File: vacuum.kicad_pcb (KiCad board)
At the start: 2 copper layers, 28 parts, among them J1 нагрузка, J2 нагрузка, J3 нагрузка, J4 геркон клапана 0, J5 геркон клапана 1, J6 геркон шибера 0, J7 геркон шибера 1, Q1 IRF740, Q2 IRF740, Q3 IRF740, SW1 Кнопка, SW2 Кнопка, SW3 Кнопка, SW4 Выключить автоматику

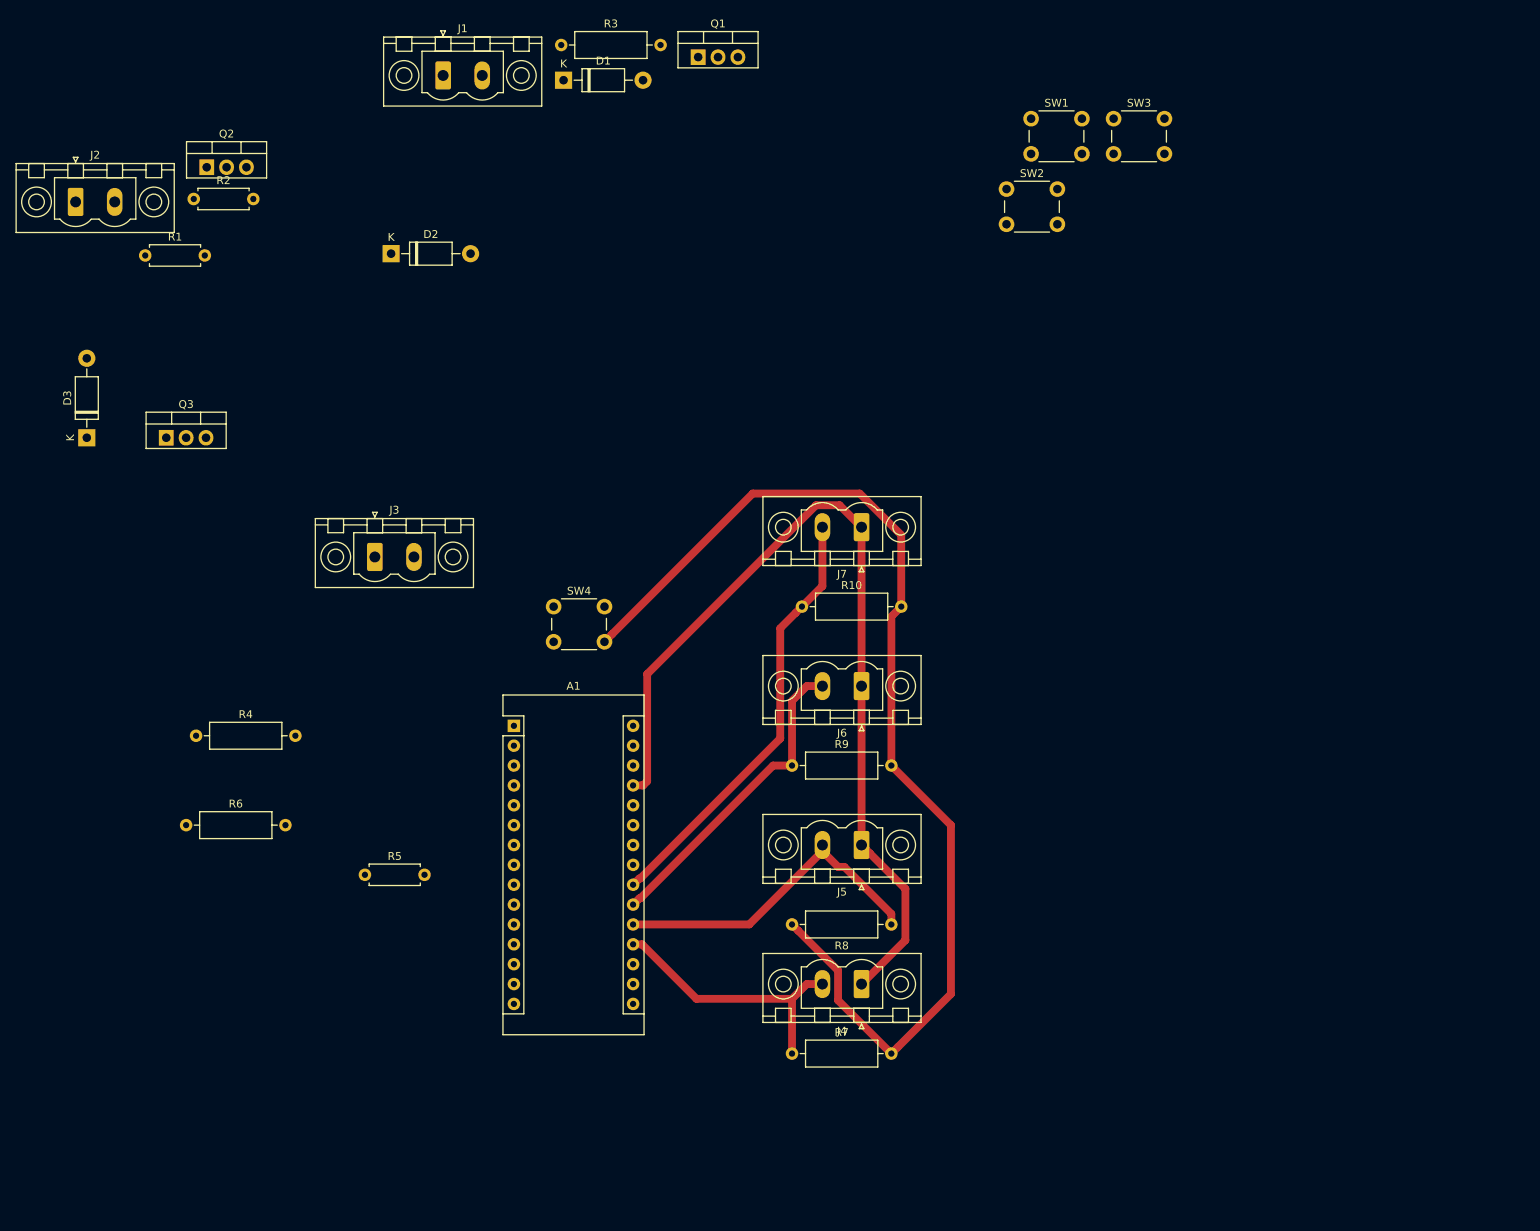
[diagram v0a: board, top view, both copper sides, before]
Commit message: common - for power supply added, terminals to power supply added
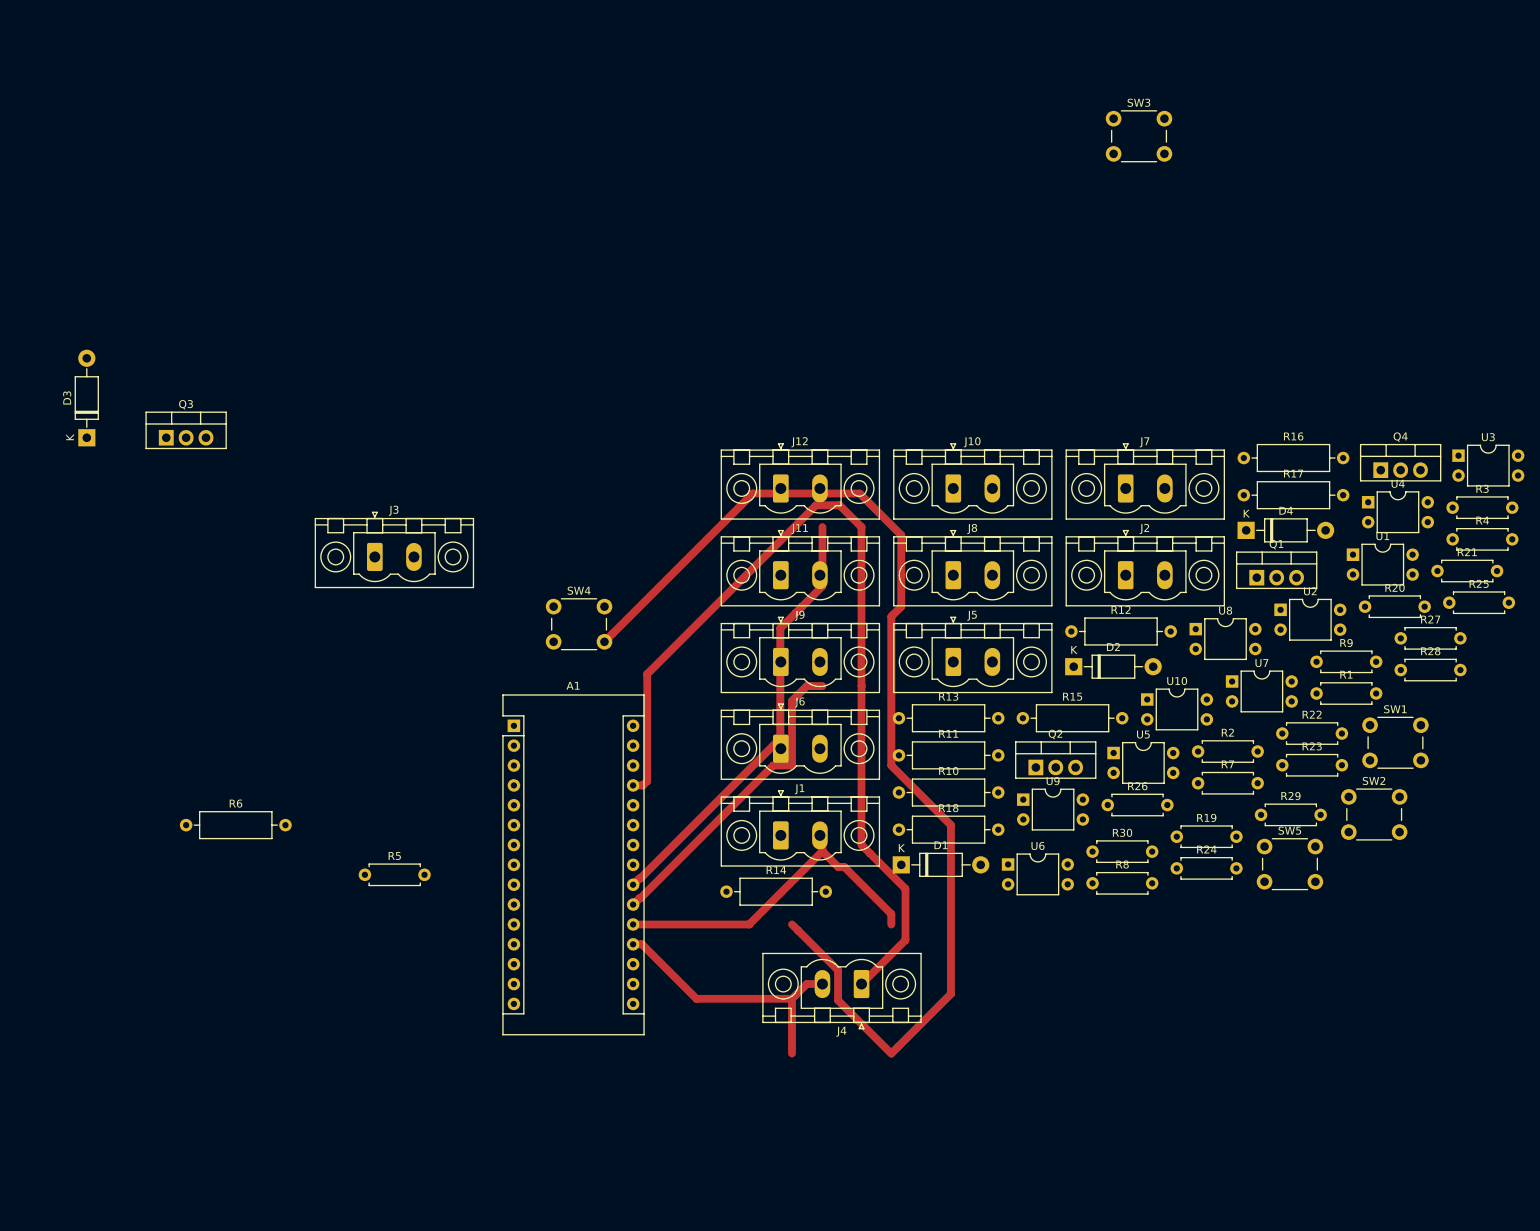
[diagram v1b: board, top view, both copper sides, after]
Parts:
- added D4: 1N4001, Diode_THT:D_DO-41_SOD81_P10.16mm_Horizontal, F.Cu at (206.7, 79.2)
- added J10: геркон шибера 1, Connector_Phoenix_MSTB:PhoenixContact_MSTBV_2,5_2-GF_1x02_P5.00mm_Vertical_ThreadedFlange, F.Cu at (169.2, 73.8)
- added J11: запасной, Connector_Phoenix_MSTB:PhoenixContact_MSTBV_2,5_2-GF_1x02_P5.00mm_Vertical_ThreadedFlange, F.Cu at (147.2, 84.9)
- added J12: запасной, Connector_Phoenix_MSTB:PhoenixContact_MSTBV_2,5_2-GF_1x02_P5.00mm_Vertical_ThreadedFlange, F.Cu at (147.2, 73.8)
- added J8: геркон клапана 1, Connector_Phoenix_MSTB:PhoenixContact_MSTBV_2,5_2-GF_1x02_P5.00mm_Vertical_ThreadedFlange, F.Cu at (169.2, 84.9)
- added J9: геркон шибера 0, Connector_Phoenix_MSTB:PhoenixContact_MSTBV_2,5_2-GF_1x02_P5.00mm_Vertical_ThreadedFlange, F.Cu at (147.2, 96.0)
- added Q4: IRF740, Package_TO_SOT_THT:TO-220-3_Vertical, F.Cu at (223.9, 71.5)
- added R11: 10k, Resistor_THT:R_Axial_DIN0309_L9.0mm_D3.2mm_P12.70mm_Horizontal, F.Cu at (162.3, 107.9)
- added R12: 10k, Resistor_THT:R_Axial_DIN0309_L9.0mm_D3.2mm_P12.70mm_Horizontal, F.Cu at (184.3, 92.1)
- added R13: 10k, Resistor_THT:R_Axial_DIN0309_L9.0mm_D3.2mm_P12.70mm_Horizontal, F.Cu at (162.3, 103.2)
- added R14: 10k, Resistor_THT:R_Axial_DIN0309_L9.0mm_D3.2mm_P12.70mm_Horizontal, F.Cu at (140.2, 125.3)
- added R15: 10k, Resistor_THT:R_Axial_DIN0309_L9.0mm_D3.2mm_P12.70mm_Horizontal, F.Cu at (178.1, 103.2)
- added R16: 10k, Resistor_THT:R_Axial_DIN0309_L9.0mm_D3.2mm_P12.70mm_Horizontal, F.Cu at (206.4, 69.9)
- added R17: 10k, Resistor_THT:R_Axial_DIN0309_L9.0mm_D3.2mm_P12.70mm_Horizontal, F.Cu at (206.4, 74.7)
- added R18: 10k, Resistor_THT:R_Axial_DIN0309_L9.0mm_D3.2mm_P12.70mm_Horizontal, F.Cu at (162.3, 117.4)
- added R19: 470, Resistor_THT:R_Axial_DIN0207_L6.3mm_D2.5mm_P7.62mm_Horizontal, F.Cu at (197.8, 118.3)
- added R20: 470, Resistor_THT:R_Axial_DIN0207_L6.3mm_D2.5mm_P7.62mm_Horizontal, F.Cu at (221.9, 88.9)
- added R21: 470, Resistor_THT:R_Axial_DIN0207_L6.3mm_D2.5mm_P7.62mm_Horizontal, F.Cu at (231.1, 84.3)
- added R22: 470, Resistor_THT:R_Axial_DIN0207_L6.3mm_D2.5mm_P7.62mm_Horizontal, F.Cu at (211.3, 105.1)
- added R23: 470, Resistor_THT:R_Axial_DIN0207_L6.3mm_D2.5mm_P7.62mm_Horizontal, F.Cu at (211.3, 109.2)
- added R24: 470, Resistor_THT:R_Axial_DIN0207_L6.3mm_D2.5mm_P7.62mm_Horizontal, F.Cu at (197.8, 122.4)
- added R25: 470, Resistor_THT:R_Axial_DIN0207_L6.3mm_D2.5mm_P7.62mm_Horizontal, F.Cu at (232.6, 88.4)
- added R26: 470, Resistor_THT:R_Axial_DIN0207_L6.3mm_D2.5mm_P7.62mm_Horizontal, F.Cu at (189.0, 114.3)
- added R27: 470, Resistor_THT:R_Axial_DIN0207_L6.3mm_D2.5mm_P7.62mm_Horizontal, F.Cu at (226.4, 93.0)
- added R28: 470, Resistor_THT:R_Axial_DIN0207_L6.3mm_D2.5mm_P7.62mm_Horizontal, F.Cu at (226.4, 97.0)
- added R29: 470, Resistor_THT:R_Axial_DIN0207_L6.3mm_D2.5mm_P7.62mm_Horizontal, F.Cu at (208.6, 115.5)
- added R30: 470, Resistor_THT:R_Axial_DIN0207_L6.3mm_D2.5mm_P7.62mm_Horizontal, F.Cu at (187.0, 120.2)
- added SW5: Кнопка, Button_Switch_THT:SW_PUSH_6mm_H5mm, F.Cu at (209.0, 119.6)
- added U1: PC817, Package_DIP:DIP-4_W7.62mm, F.Cu at (220.3, 82.3)
- added U10: PC817, Package_DIP:DIP-4_W7.62mm, F.Cu at (194.0, 100.8)
- added U2: PC817, Package_DIP:DIP-4_W7.62mm, F.Cu at (211.1, 89.3)
- added U3: PC817, Package_DIP:DIP-4_W7.62mm, F.Cu at (233.8, 69.6)
- added U4: PC817, Package_DIP:DIP-4_W7.62mm, F.Cu at (222.3, 75.6)
- added U5: PC817, Package_DIP:DIP-4_W7.62mm, F.Cu at (189.7, 107.6)
- added U6: PC817, Package_DIP:DIP-4_W7.62mm, F.Cu at (176.2, 121.9)
- added U7: PC817, Package_DIP:DIP-4_W7.62mm, F.Cu at (204.9, 98.5)
- added U8: PC817, Package_DIP:DIP-4_W7.62mm, F.Cu at (200.2, 91.8)
- added U9: PC817, Package_DIP:DIP-4_W7.62mm, F.Cu at (178.2, 113.6)
- J1: value нагрузка -> к БП
- J5: value геркон клапана 1 -> нагрузка
- J6: value геркон шибера 0 -> нагрузка
- J7: value геркон шибера 1 -> к БП
- R1, R2, R5: value 100 -> 470
- R3, R4, R7, R8, R9: value 10k -> 470; footprint Resistor_THT:R_Axial_DIN0309_L9.0mm_D3.2mm_P12.70mm_Horizontal -> Resistor_THT:R_Axial_DIN0207_L6.3mm_D2.5mm_P7.62mm_Horizontal
- moved R4 162.6 mm to (233.1, 80.3)
- moved R1 159.9 mm to (215.7, 100.0)
- moved R2 146.6 mm to (200.5, 107.4)
- moved J2 142.5 mm to (191.3, 84.9)
- moved Q2 130.9 mm to (179.8, 109.5)
- moved R3 128.4 mm to (233.1, 76.2)
- moved D1 109.2 mm to (162.6, 121.9)
- moved J1 106.3 mm to (147.2, 118.2)
- moved D2 102.0 mm to (184.6, 96.6)
- moved Q1 97.6 mm to (208.0, 85.2)
- moved SW2 89.2 mm to (219.8, 113.2)
- moved SW1 88.8 mm to (222.5, 104.1)
- moved R9 68.4 mm to (215.7, 96.0)
- moved R7 62.4 mm to (200.5, 111.5)
- moved J7 34.1 mm to (191.3, 73.8), turned to 0 degrees
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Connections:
- A1 pad 19: Net-(A1-Pad19) -> (no net)
- A1 pad 23: (no net) -> Net-(A1-Pad23)
- A1 pad 24: (no net) -> Net-(A1-Pad24)
- A1 pad 25: (no net) -> Net-(A1-Pad25)
- A1 pad 4: Earth -> Net-(A1-Pad4)
- A1 pad 6: (no net) -> Net-(A1-Pad6)
- D2 pad 1: Net-(D2-Pad1) -> Net-(D1-Pad1)
- D3 pad 2: Net-(D2-Pad1) -> Net-(D3-Pad2)
- J1 pad 1: +24V -> Earth
- J1 pad 2: Net-(D1-Pad2) -> +24V
- J2 pad 2: Net-(D2-Pad2) -> Net-(D1-Pad2)
- J3 pad 2: Net-(D2-Pad1) -> Net-(D3-Pad2)
- J4 pad 1: +5V -> Net-(J4-Pad1)
- J4 pad 2: Net-(A1-Pad19) -> Earth
- J5 pad 1: +5V -> +24V
- J5 pad 2: Net-(A1-Pad20) -> Net-(D2-Pad2)
- J6 pad 1: +5V -> +24V
- J6 pad 2: Net-(A1-Pad21) -> Net-(D4-Pad2)
- J7 pad 1: +5V -> Earth
- J7 pad 2: Net-(A1-Pad22) -> +5V
- Q2 pad 3: Net-(D2-Pad1) -> Net-(D1-Pad1)
- Q3 pad 2: Net-(D2-Pad1) -> Net-(D3-Pad2)
- R1 pad 2: Net-(A1-Pad9) -> +5V
- R10 pad 1: Net-(A1-Pad22) -> Net-(A1-Pad6)
- R10 pad 2: Earth -> Net-(A1-Pad4)
- R2 pad 2: Net-(A1-Pad11) -> +5V
- R3 pad 1: Net-(A1-Pad9) -> Net-(Q4-Pad1)
- R3 pad 2: Net-(D1-Pad1) -> +5V
- R4 pad 1: Net-(A1-Pad11) -> Net-(R4-Pad1)
- R4 pad 2: Net-(D2-Pad1) -> Net-(A1-Pad6)
- R5 pad 2: Net-(A1-Pad13) -> +5V
- R6 pad 2: Net-(D1-Pad1) -> Net-(A1-Pad4)
- R7 pad 1: Net-(A1-Pad19) -> Net-(R7-Pad1)
- R7 pad 2: Earth -> Net-(A1-Pad9)
- R8 pad 1: Net-(A1-Pad20) -> Net-(R8-Pad1)
- R8 pad 2: Earth -> Net-(A1-Pad11)
- R9 pad 1: Net-(A1-Pad21) -> Net-(R9-Pad1)
- R9 pad 2: Earth -> Net-(A1-Pad13)
- SW2 pad 1: Net-(D2-Pad1) -> Earth
- SW3 pad 2: Net-(D2-Pad1) -> Net-(D3-Pad2)

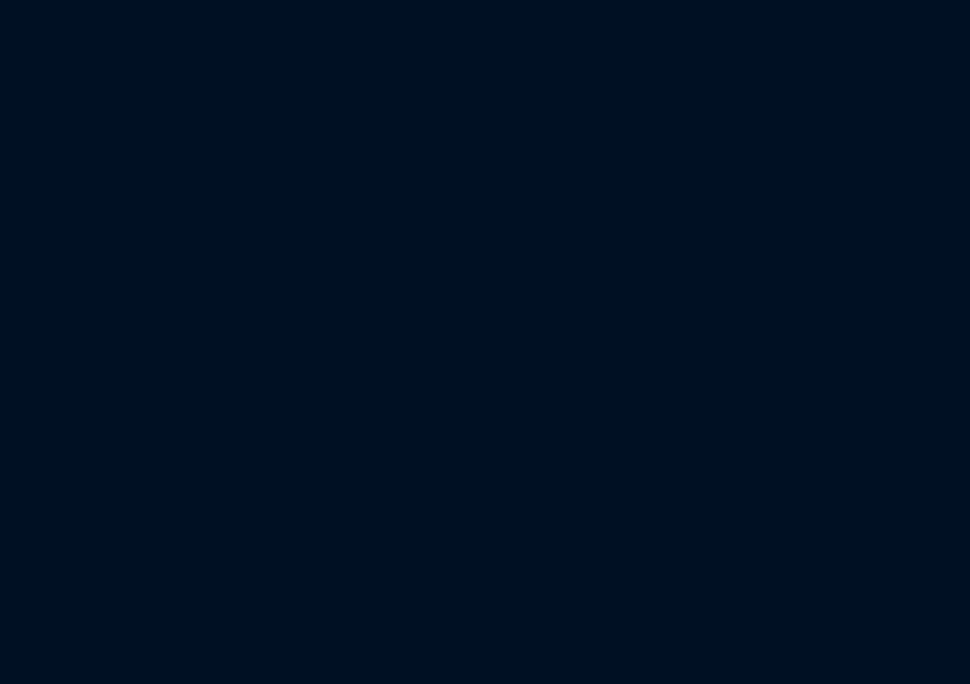
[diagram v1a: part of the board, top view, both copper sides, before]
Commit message: some connectors for power supply added
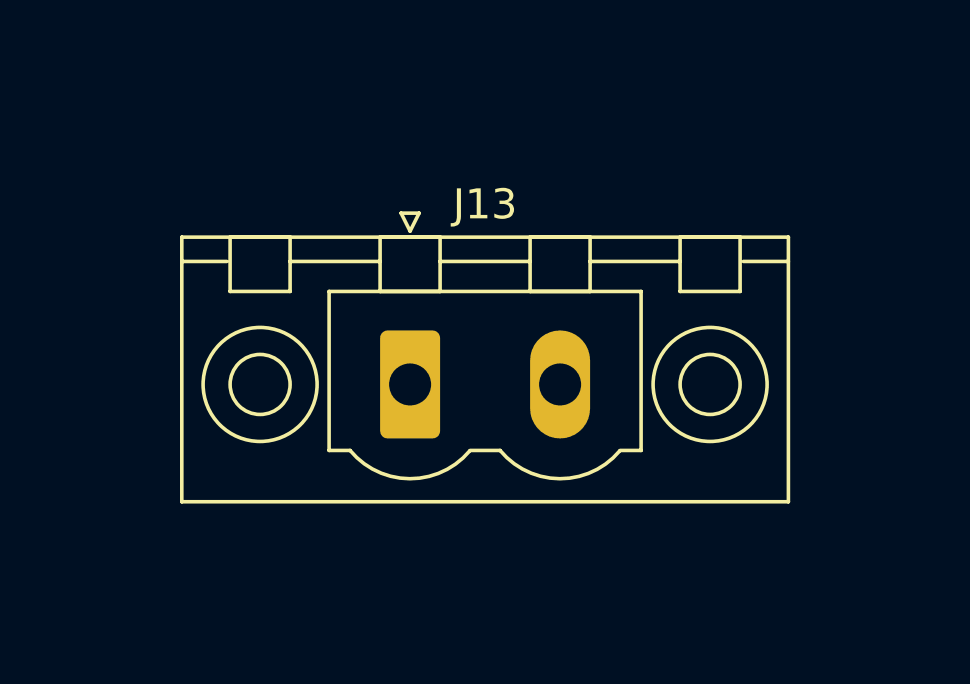
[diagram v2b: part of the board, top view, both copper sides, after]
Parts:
- added J13: к БП, Connector_Phoenix_MSTB:PhoenixContact_MSTBV_2,5_2-GF_1x02_P5.00mm_Vertical_ThreadedFlange, F.Cu at (139.7, 34.3)
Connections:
- A1 pad 4: Net-(A1-Pad4) -> Earth
- R10 pad 2: Net-(A1-Pad4) -> Earth
- R11 pad 2: Net-(A1-Pad4) -> Earth
- R12 pad 2: Net-(A1-Pad4) -> Earth
- R13 pad 2: Net-(A1-Pad4) -> Earth
- R14 pad 2: Net-(A1-Pad4) -> Earth
- R15 pad 2: Net-(A1-Pad4) -> Earth
- R16 pad 2: Net-(A1-Pad4) -> Earth
- R17 pad 2: Net-(A1-Pad4) -> Earth
- R18 pad 2: Net-(A1-Pad4) -> Earth
- R6 pad 2: Net-(A1-Pad4) -> Earth
- U1 pad 2: Net-(A1-Pad4) -> Earth
- U2 pad 2: Net-(A1-Pad4) -> Earth
- U3 pad 2: Net-(A1-Pad4) -> Earth
- U4 pad 2: Net-(A1-Pad4) -> Earth
